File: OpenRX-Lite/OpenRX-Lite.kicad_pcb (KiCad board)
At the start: 2 copper layers, 0 parts

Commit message: Unify library tables, import RFX2401C, Lite schematic capture
- All 6 projects now share OpenRX-Shared + OpenRX-Lite lib tables
- Import RFX2401C (C19213) into shared library with 3D model path fix
- OpenRX-Lite schematic: 0 ERC errors (captured in KiCad GUI)
- Add .gitignore for .lck and .history files
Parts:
- added AE1: 2450AT18A100E, OpenRX-Shared:ANT-SMD_L3.2-W1.6, F.Cu at (173.2, 105.3)
- added AE2: 47948-0001, OpenRX-Shared:ANT-SMD_47948-0001, F.Cu at (172.8, 101.4)
- added C1: 100nF, Capacitor_SMD:C_0201_0603Metric, F.Cu at (162.1, 89.6)
- added C10: 1uF, Capacitor_SMD:C_0201_0603Metric, F.Cu at (164.5, 94.9)
- added C11: 10uF, Capacitor_SMD:C_0201_0603Metric, F.Cu at (164.5, 96.6)
- added C12: 10uF, Capacitor_SMD:C_0201_0603Metric, F.Cu at (164.5, 98.4)
- added C13: 100nF, Capacitor_SMD:C_0201_0603Metric, F.Cu at (167.0, 89.6)
- added C14: 100nF, Capacitor_SMD:C_0201_0603Metric, F.Cu at (167.0, 91.4)
- added C15: 100nF, Capacitor_SMD:C_0201_0603Metric, F.Cu at (167.0, 93.1)
- added C16: 470nF, Capacitor_SMD:C_0201_0603Metric, F.Cu at (167.0, 94.9)
- added C17: 100nF, Capacitor_SMD:C_0201_0603Metric, F.Cu at (167.0, 96.6)
- added C18: 1nF, Capacitor_SMD:C_0201_0603Metric, F.Cu at (167.0, 98.4)
- added C19: 1uF, Capacitor_SMD:C_0201_0603Metric, F.Cu at (169.4, 89.6)
- added C2: 100nF, Capacitor_SMD:C_0201_0603Metric, F.Cu at (162.1, 91.4)
- added C3: 100nF, Capacitor_SMD:C_0201_0603Metric, F.Cu at (162.1, 93.1)
- added C4: 100nF, Capacitor_SMD:C_0201_0603Metric, F.Cu at (162.1, 94.9)
- added C5: 100nF, Capacitor_SMD:C_0201_0603Metric, F.Cu at (162.1, 96.6)
- added C6: 10pF, Capacitor_SMD:C_0201_0603Metric, F.Cu at (162.1, 98.4)
- added C7: 10pF, Capacitor_SMD:C_0201_0603Metric, F.Cu at (164.5, 89.6)
- added C8: 1uF, Capacitor_SMD:C_0201_0603Metric, F.Cu at (164.5, 91.4)
- added C9: 1uF, Capacitor_SMD:C_0201_0603Metric, F.Cu at (164.5, 93.1)
- added D1: XL-1010RGBC-WS2812B, OpenRX-Shared:LED-SMD_4P-L1.0-W1.0-TL_XL-1010RGBC-WS2812B, F.Cu at (168.3, 106.8)
- added OSC1: OW7EL89CENUNFAYLC-52M, OpenRX-Shared:OSC-SMD_4P-L2.0-W1.6-BL_TXC_7Z, F.Cu at (172.9, 96.9)
- added R1: 10k, Resistor_SMD:R_0201_0603Metric, F.Cu at (169.4, 91.4)
- added R2: 10k, Resistor_SMD:R_0201_0603Metric, F.Cu at (169.4, 93.1)
- added R3: 10k, Resistor_SMD:R_0201_0603Metric, F.Cu at (169.4, 94.9)
- added R4: 10k, Resistor_SMD:R_0201_0603Metric, F.Cu at (169.4, 96.6)
- added TP1: RX, OpenRX-Shared:SolderPad_1.0x1.5mm, F.Cu at (162.1, 100.7)
- added TP2: TX, OpenRX-Shared:SolderPad_1.0x1.5mm, F.Cu at (164.5, 100.7)
- added TP3: 5V, OpenRX-Shared:SolderPad_1.0x1.5mm, F.Cu at (167.0, 100.7)
- added TP4: GND, OpenRX-Shared:SolderPad_1.0x1.5mm, F.Cu at (169.4, 100.7)
- added U1: ESP32-C3FH4, OpenRX-Shared:QFN-32_L5.0-W5.0-P0.50-TL-EP3.7, F.Cu at (174.3, 92.1)
- added U2: TLV75533PDQNR, OpenRX-Shared:X2SON-4_L1.0-W1.0-P0.65-TL-EP, F.Cu at (176.4, 100.4)
- added U3: SX1281IMLTRT, OpenRX-Shared:QFN-24_L4.0-W4.0-P0.50-TL-EP2.6, F.Cu at (163.8, 105.1)
- added USB1: DEA102700LT-6307A2, OpenRX-Shared:FILTER-SMD_4P-L1.0-W0.5-L_DEA102700LT-XXX, F.Cu at (176.4, 96.5)
- added X1: CJ17-400001010B20, OpenRX-Shared:CRYSTAL-SMD_4P-L1.6-W1.2-BL, F.Cu at (168.6, 103.7)

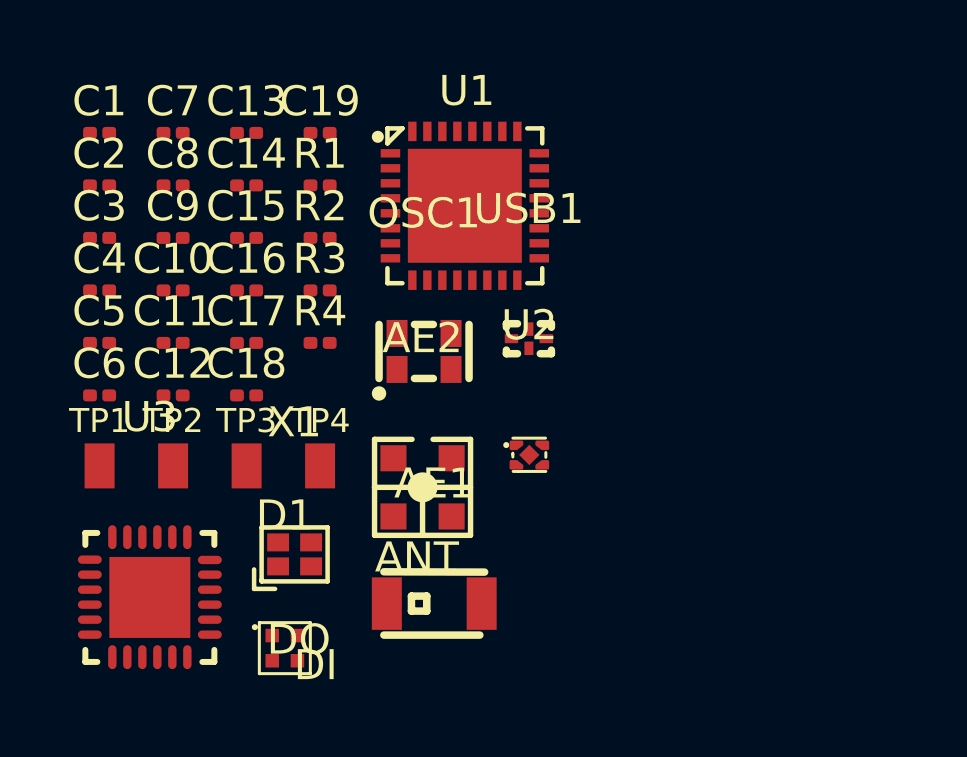
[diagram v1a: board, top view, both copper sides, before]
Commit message: Fix Gemini crystal load caps to 18pF (C62164), matching Lite and Mono
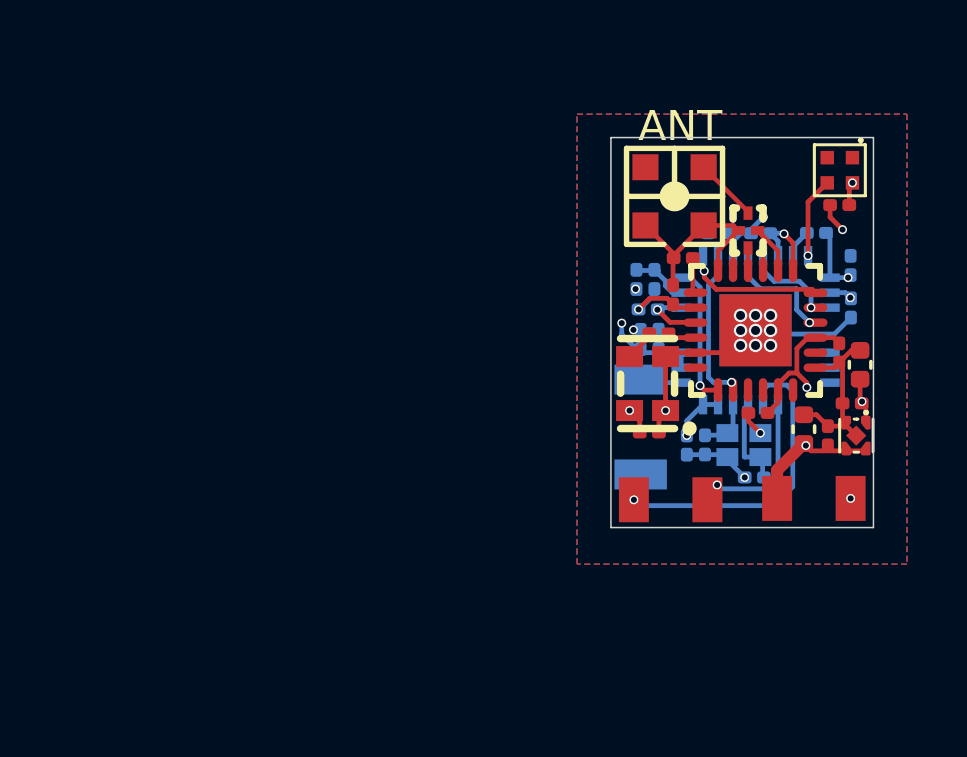
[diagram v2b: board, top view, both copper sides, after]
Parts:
- added C20: 100nF, Capacitor_SMD:C_0201_0603Metric, F.Cu at (186.8, 92.0)
- AE1, C1, C19, C2, C3, C4, C5, C8, R1, R2, R3, R4, U1, X1: moved to B.Cu
- C11, C12: footprint Capacitor_SMD:C_0201_0603Metric -> Capacitor_SMD:C_0402_1005Metric
- C6, C7: value 10pF -> 18pF; moved to B.Cu
- moved C3 25.2 mm to (187.1, 95.5), turned to -90 degrees
- moved C4 25.0 mm to (187.1, 94.0), turned to 90 degrees
- moved D1 24.4 mm to (186.8, 90.9), turned to -90 degrees
- moved C10 22.9 mm to (187.2, 98.6), turned to 180 degrees
- moved C11 22.9 mm to (187.4, 97.4), turned to 90 degrees
- moved C9 22.8 mm to (186.4, 99.7), turned to 90 degrees
- moved C7 22.5 mm to (183.9, 101.1), turned to 180 degrees
- moved U3 22.1 mm to (183.9, 96.2)
- moved C12 21.1 mm to (185.6, 99.5), turned to 90 degrees
- moved C5 20.9 mm to (182.7, 93.0), turned to 180 degrees
- moved C14 20.5 mm to (186.7, 97.0), turned to -90 degrees
- moved TP1 20.3 mm to (182.3, 101.9), turned to 180 degrees
- moved C6 20.2 mm to (182.3, 100.0), turned to -90 degrees
- moved C1 19.9 mm to (180.7, 96.5), turned to 90 degrees
- moved C2 18.8 mm to (180.1, 96.5), turned to 90 degrees
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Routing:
- net GND: track 0.00 -> 31.6 mm, vias 0 -> 16
- net +3V3: track 0.00 -> 21.1 mm, vias 0 -> 9
- net +5V: track 0.00 -> 14.8 mm, vias 0 -> 2
- net Net-(U1-U0TXD): track 0.00 -> 10.5 mm, vias 0 -> 1
- net /ESP32-C3 + SX1281 Core/DIO1: track 0.00 -> 5.30 mm, vias 0 -> 1
- net Net-(U1-U0RXD): track 0.00 -> 4.76 mm, vias 0 -> 1
- net /ESP32-C3 + SX1281 Core/BUSY: track 0.00 -> 4.70 mm, vias 0 -> 1
- net /ESP32-C3 + SX1281 Core/SCK: track 0.00 -> 4.66 mm, vias 0 -> 1
- net /ESP32-C3 + SX1281 Core/MISO: track 0.00 -> 3.98 mm, vias 0 -> 1
- net /ESP32-C3 + SX1281 Core/XTAL_N: track 0.00 -> 3.09 mm
- net /ESP32-C3 + SX1281 Core/MOSI: track 0.00 -> 3.04 mm, vias 0 -> 1
- net /ESP32-C3 + SX1281 Core/LED: track 0.00 -> 2.70 mm, vias 0 -> 1
- net /ESP32-C3 + SX1281 Core/NSS: track 0.00 -> 2.66 mm, vias 0 -> 1
- net /ESP32-C3 + SX1281 Core/RST: track 0.00 -> 2.25 mm, vias 0 -> 1
- net Net-(USB1-OUT): track 0.00 -> 2.14 mm
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- added copper zone on In1.Cu, net +3V3
- added copper zone on B.Cu, net GND
- added copper zone on F.Cu, net GND
- added copper zone on In2.Cu, net GND
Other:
- board outline added: 8.8 x 13 mm
- copper layers 2 -> 4

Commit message: Repo cleanup: final state for handoff
- Clean README with architecture, BOM, CE notes, status
- Remove dated analysis files (absorbed into FINAL_NETLIST + KICAD_WORKFLOW)
- Remove stale OpenRX-Dual (archived), ERC reports, backups, prl files
- Updated .gitignore for .kicad_dru, production backups
- CERN-OHL-S v2 license confirmed
- 3 active projects: Lite, Mono, Gemini
- Schematics final, initial PCB layouts done, routing in progress
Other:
- copper layers 4 -> 6
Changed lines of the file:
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@@
 	(generator_version "10.0")
 	(general
-		(thickness 1.0278)
+		(thickness 1.0)
 		(legacy_teardrops no)
 	)
@@
 		(4 "In1.Cu" signal)
 		(6 "In2.Cu" signal)
+		(8 "In3.Cu" signal)
+		(10 "In4.Cu" signal)
 		(2 "B.Cu" signal)
 		(9 "F.Adhes" user "F.Adhesive")
@@
 			(layer "dielectric 2"
 				(type "core")
-				(thickness 0.7074)
+				(thickness 0.16)
 				(material "FR4")
 				(epsilon_r 4.5)
@@
 			(layer "dielectric 3"
 				(type "prepreg")
+				(thickness 0.3292)
+				(material "FR4")
+				(epsilon_r 4.5)
+				(loss_tangent 0.02)
+			)
+			(layer "In3.Cu"
+				(type "copper")
+				(thickness 0.0152)
+			)
+			(layer "dielectric 4"
+				(type "core")
+				(thickness 0.16)
+				(material "FR4")
+				(epsilon_r 4.5)
+				(loss_tangent 0.02)
+			)
+			(layer "In4.Cu"
+				(type "copper")
+				(thickness 0.0152)
+			)
+			(layer "dielectric 5"
+				(type "prepreg")
 				(thickness 0.1)
